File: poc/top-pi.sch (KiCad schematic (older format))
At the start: 124 parts

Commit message: Upgrade to newer kicad
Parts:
- 25MHz: symbol Crystal -> poc-rescue:Crystal
- C? (x98): symbol C_Small -> poc-rescue:C_Small
- D? (x2): symbol LED -> poc-rescue:LED
- J? (x2): symbol Micro_SD_Card -> poc-rescue:Micro_SD_Card
- J? (x2): symbol USB_A_x2 -> usb_a_x2:USB_A_x2
- J?: symbol Conn_01x05 -> poc-rescue:Conn_01x05
- L? (x4): symbol L_Core_Ferrite -> poc-rescue:L_Core_Ferrite
- R? (x10): symbol R -> poc-rescue:R
- TopPi? (x2): symbol RPI_CM3L -> cm3l:RPI_CM3L
- U? (x2): symbol LAN9512 -> LAN9512:LAN9512

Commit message: wire SD card to cm3l
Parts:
- removed J?: Micro_SD_Card, symbol poc-rescue:Micro_SD_Card
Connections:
- net GND: now also TopPi?.168 (USB_OTGID), TopPi?.168 (USB_OTGID)
- net at TopPi?.10 (SDX_CLK), TopPi?.10 (SDX_CLK): now also J?.5 (CLK)
- net at TopPi?.12 (SDX_CMD), TopPi?.12 (SDX_CMD): now also J?.3 (CMD)
- net at TopPi?.16 (SDX_D0), TopPi?.16 (SDX_D0): now also J?.7 (DAT0)
- net at TopPi?.18 (SDX_D1), TopPi?.18 (SDX_D1): now also J?.8 (DAT1)
- net at TopPi?.22 (SDX_D2), TopPi?.22 (SDX_D2): now also J?.1 (DAT2)
- net at TopPi?.24 (SDX_D3), TopPi?.24 (SDX_D3): now also J?.2 (DAT3/CD)
- no-connect marks 15 -> 17
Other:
- moved on the sheet: J?

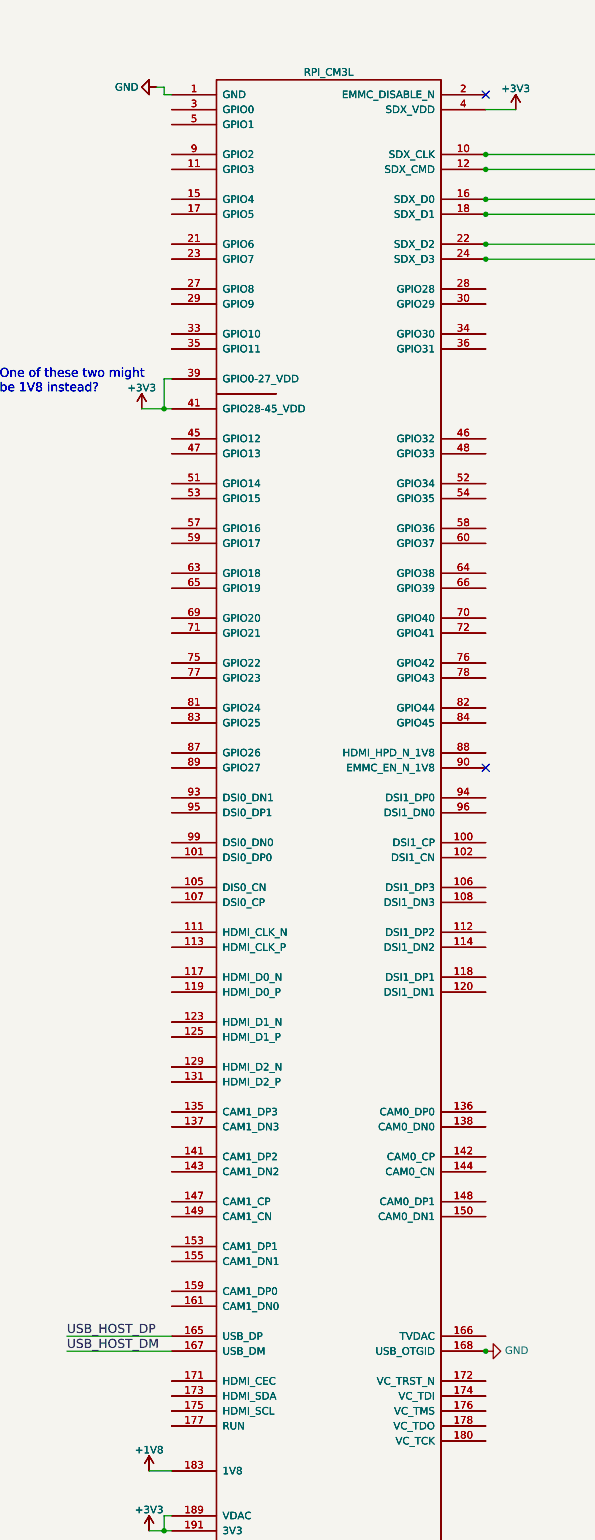
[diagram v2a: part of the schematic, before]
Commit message: CM3L GPIO pins: only 14/15 for UART
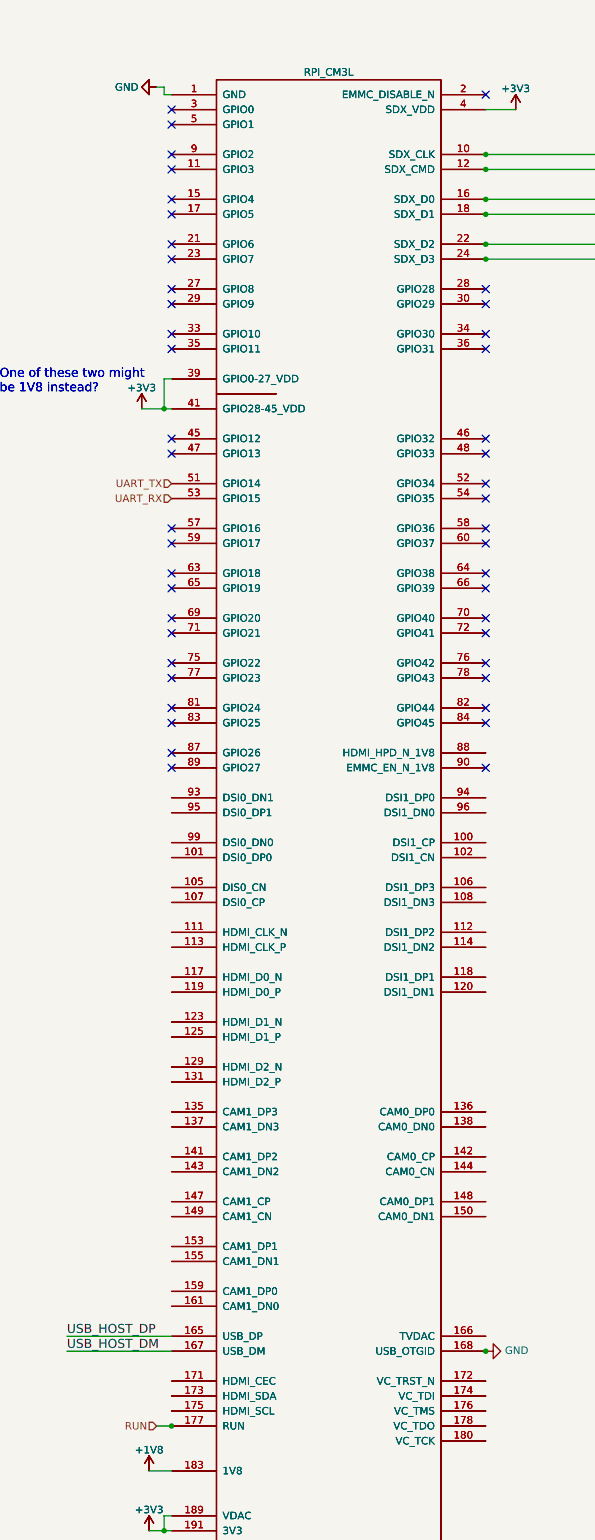
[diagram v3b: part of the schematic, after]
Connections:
- net RUN: now reaches TopPi?.177 (RUN), TopPi?.177 (RUN)
- net UART_TX: now reaches TopPi?.51 (GPIO14), TopPi?.51 (GPIO14)
- net UART_RX: now reaches TopPi?.53 (GPIO15), TopPi?.53 (GPIO15)
- no-connect marks 17 -> 61
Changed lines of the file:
@@
 NoConn ~ 12100 2000
 NoConn ~ 12100 6500
+Text HLabel 9900 10900 0    50   Input ~ 0
+RUN
+Wire Wire Line
+	9900 10900 10000 10900
+Connection ~ 10000 10900
+Text HLabel 10000 4600 0    50   Input ~ 0
+UART_TX
+Text HLabel 10000 4700 0    50   Input ~ 0
+UART_RX
+NoConn ~ 10000 2100
+NoConn ~ 10000 2200
+NoConn ~ 10000 2400
+NoConn ~ 10000 2500
+NoConn ~ 10000 2700
+NoConn ~ 10000 2800
+NoConn ~ 10000 3000
+NoConn ~ 10000 3100
+NoConn ~ 10000 3300
+NoConn ~ 10000 3400
+NoConn ~ 10000 3600
+NoConn ~ 10000 3700
+NoConn ~ 10000 4300
+NoConn ~ 10000 4400
+NoConn ~ 10000 4900
+NoConn ~ 10000 5000
+NoConn ~ 10000 5200
+NoConn ~ 10000 5300
+NoConn ~ 10000 5500
+NoConn ~ 10000 5600
+NoConn ~ 10000 5800
+NoConn ~ 10000 5900
+NoConn ~ 10000 6100
+NoConn ~ 10000 6200
+NoConn ~ 10000 6400
+NoConn ~ 10000 6500
+NoConn ~ 12100 3300
+NoConn ~ 12100 3400
+NoConn ~ 12100 3600
+NoConn ~ 12100 3700
+NoConn ~ 12100 4300
+NoConn ~ 12100 4400
+NoConn ~ 12100 4600
+NoConn ~ 12100 4700
+NoConn ~ 12100 4900
+NoConn ~ 12100 5000
+NoConn ~ 12100 5200
+NoConn ~ 12100 5300
+NoConn ~ 12100 5500
+NoConn ~ 12100 5600
+NoConn ~ 12100 5800
+NoConn ~ 12100 5900
+NoConn ~ 12100 6100
+NoConn ~ 12100 6200
 $EndSCHEMATC

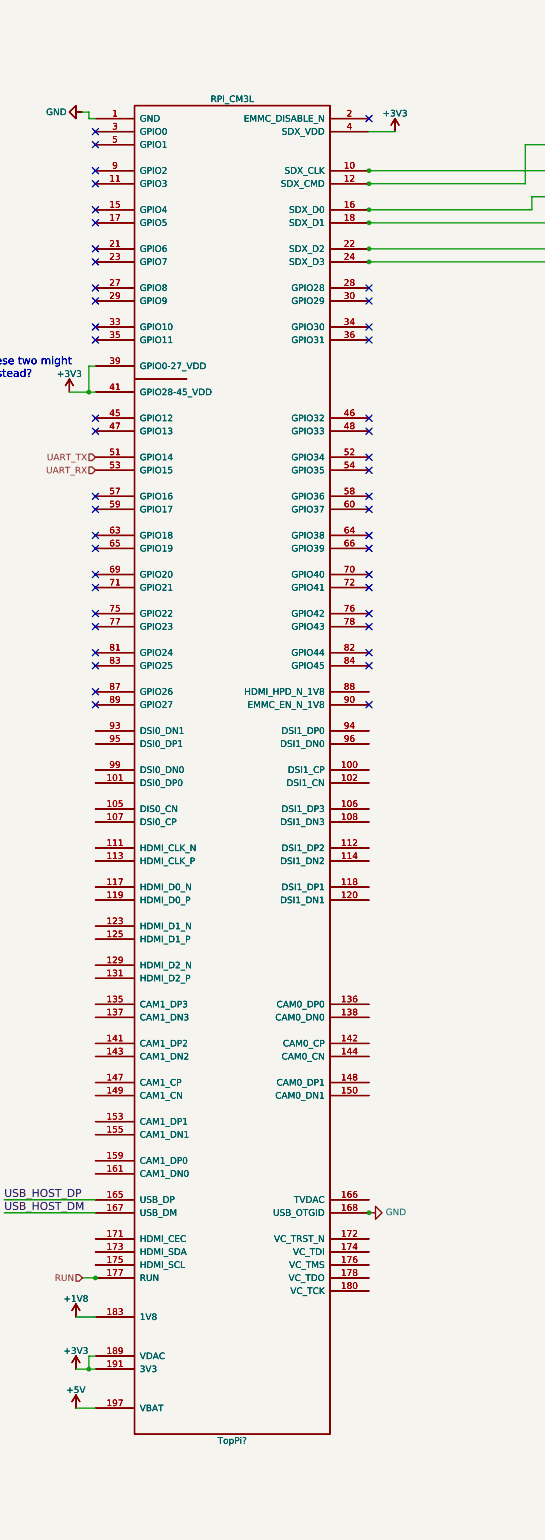
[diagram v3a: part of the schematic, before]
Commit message: Remaining CM3L pins, incl. jtag header
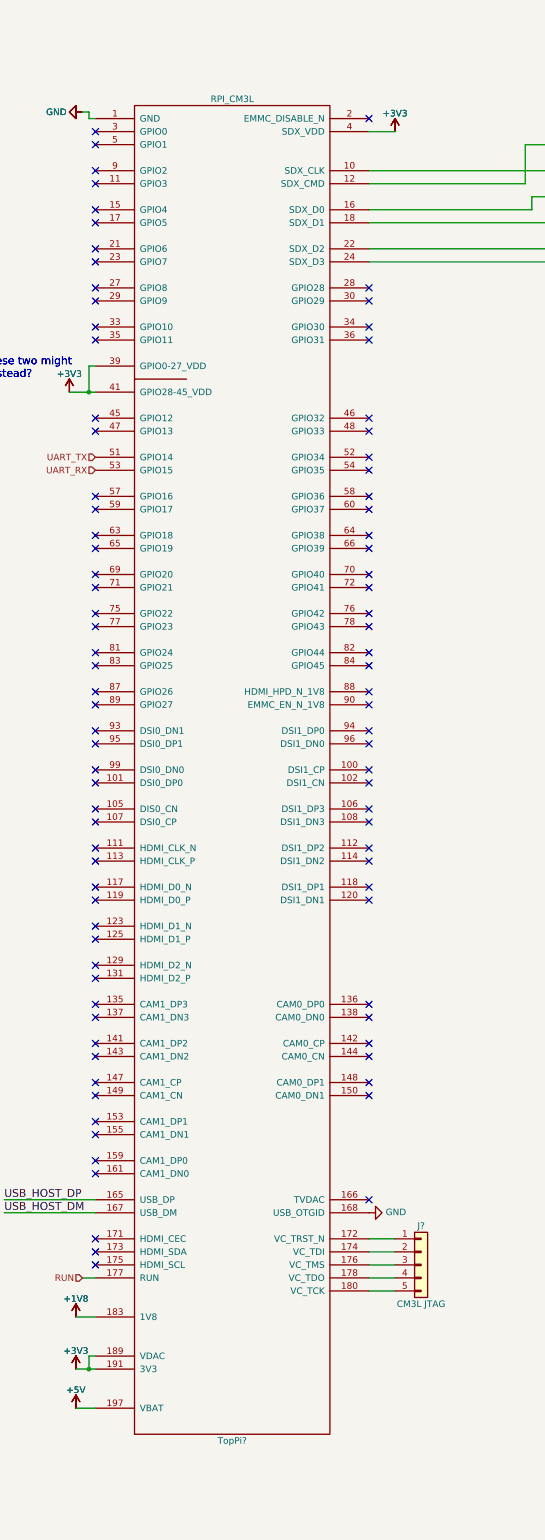
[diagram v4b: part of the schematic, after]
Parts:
- removed TopPi?: RPI_CM3L, symbol cm3l:RPI_CM3L
- added J?: CM3L JTAG, symbol poc-rescue:Conn_01x05
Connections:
- net at TopPi?.172 (VC_TRST_N): now also J?.1 (Pin_1)
- net at TopPi?.174 (VC_TDI): now also J?.2 (Pin_2)
- net at TopPi?.176 (VC_TMS): now also J?.3 (Pin_3)
- net at TopPi?.178 (VC_TDO): now also J?.4 (Pin_4)
- net at TopPi?.180 (VC_TCK): now also J?.5 (Pin_5)
- no-connect marks 61 -> 106
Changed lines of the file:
@@
-$EndComp
-$Comp
-L cm3l:RPI_CM3L TopPi?
-U 1 1 59910A99
-P 11050 7050
-F 0 "TopPi?" H 11050 1950 50  0000 C CNN
-F 1 "RPI_CM3L" H 11050 12250 50  0000 C CNN
-F 2 "" H 11050 7050 50  0001 C CNN
-F 3 "" H 11050 7050 50  0001 C CNN
-	1    11050 7050
-	1    0    0    -1
 $EndComp
 $Comp
@@
 Wire Wire Line
 	7300 12900 7300 13100
-Connection ~ 12100 2400
 Wire Wire Line
 	12100 2500 13300 2500
-Connection ~ 12100 2500
 Wire Wire Line
 	12100 2400 14150 2400
@@
 Wire Wire Line
 	13350 2600 14150 2600
-Connection ~ 12100 2700
 Wire Wire Line
 	12100 2800 13450 2800
@@
 Wire Wire Line
 	13450 2700 14150 2700
-Connection ~ 12100 2800
 Wire Wire Line
 	12100 3000 13550 3000
@@
 Wire Wire Line
 	13550 2000 14150 2000
-Connection ~ 12100 3000
 Wire Wire Line
 	12100 3100 13650 3100
@@
 Wire Wire Line
 	13650 2100 14150 2100
-Connection ~ 12100 3100
 $Comp
 L power:GND #PWR?
@@
 	0    -1   -1   0
 $EndComp
-Connection ~ 12100 10400
 NoConn ~ 12100 2000
 NoConn ~ 12100 6500
@@
 Wire Wire Line
 	9900 10900 10000 10900
-Connection ~ 10000 10900
 Text HLabel 10000 4600 0    50   Input ~ 0
 UART_TX
@@
 NoConn ~ 12100 6100
 NoConn ~ 12100 6200
+NoConn ~ 10000 6700
+NoConn ~ 10000 6800
+NoConn ~ 10000 7000
+NoConn ~ 10000 7100
+NoConn ~ 10000 7300
+NoConn ~ 10000 7400
+NoConn ~ 10000 7600
+NoConn ~ 10000 7700
+NoConn ~ 10000 7900
+NoConn ~ 10000 8000
+NoConn ~ 10000 8200
+NoConn ~ 10000 8300
+NoConn ~ 10000 8500
+NoConn ~ 10000 8600
+NoConn ~ 10000 8800
+NoConn ~ 10000 8900
+NoConn ~ 10000 9100
+NoConn ~ 10000 9200
+NoConn ~ 10000 9400
+NoConn ~ 10000 9500
+NoConn ~ 10000 9700
+NoConn ~ 10000 9800
+NoConn ~ 10000 10000
+NoConn ~ 10000 10100
+NoConn ~ 10000 10600
+NoConn ~ 10000 10700
+NoConn ~ 10000 10800
+NoConn ~ 12100 6400
+NoConn ~ 12100 6700
+NoConn ~ 12100 6800
+NoConn ~ 12100 7000
+NoConn ~ 12100 7100
+NoConn ~ 12100 7300
+NoConn ~ 12100 7400
+NoConn ~ 12100 7600
+NoConn ~ 12100 7700
+NoConn ~ 12100 7900
+NoConn ~ 12100 8000
+NoConn ~ 12100 8800
+NoConn ~ 12100 8900
+NoConn ~ 12100 9100
+NoConn ~ 12100 9200
+NoConn ~ 12100 9400
+NoConn ~ 12100 9500
+NoConn ~ 12100 10300
+$Comp
+L poc-rescue:Conn_01x05 J?
+U 1 1 5DE691E5
+P 12500 10800
+F 0 "J?" H 12500 11100 50  0000 C CNN
+F 1 "CM3L JTAG" H 12500 10500 50  0000 C CNN
+F 2 "" H 12500 10800 50  0001 C CNN
+F 3 "" H 12500 10800 50  0001 C CNN
+	1    12500 10800
+	1    0    0    -1
+$EndComp
+Wire Wire Line
+	12100 10600 12300 10600
+Wire Wire Line
+	12100 10700 12300 10700
+Wire Wire Line
+	12100 10800 12300 10800
+Wire Wire Line
+	12100 10900 12300 10900
+Wire Wire Line
+	12100 11000 12300 11000
 $EndSCHEMATC
